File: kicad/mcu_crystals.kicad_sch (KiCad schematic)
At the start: 4 parts, among them X1 32MHz, X2 32kHz768

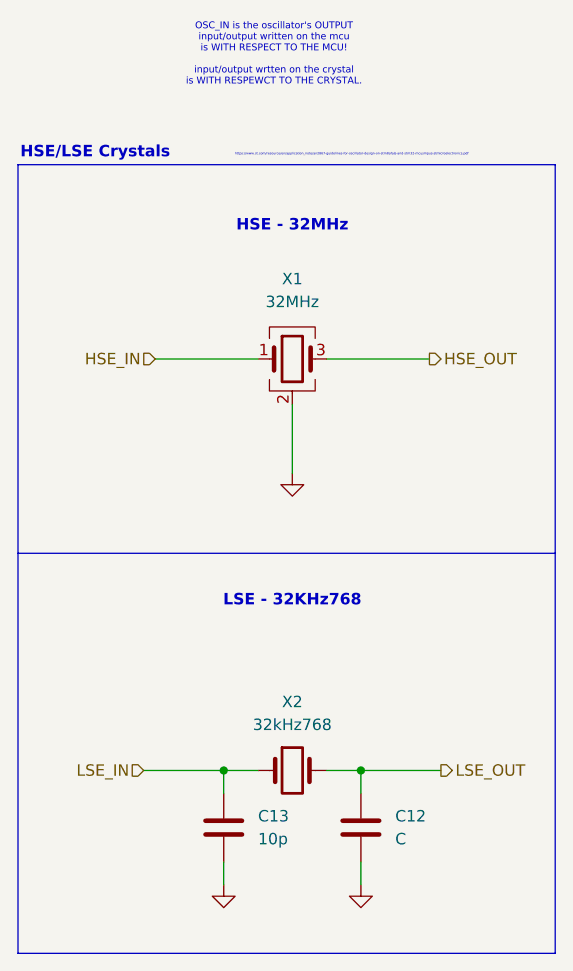
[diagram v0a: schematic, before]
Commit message: refactor(schematic): polish the schematic as much as possible - add new Basmala - fix netlist names almost EVERYWHERE, this is to help with net classes, and to help with building a good habit of naming nets properly - add a 100n capacitor to the SWD connector power pin - update many many other things EVERYWHERE
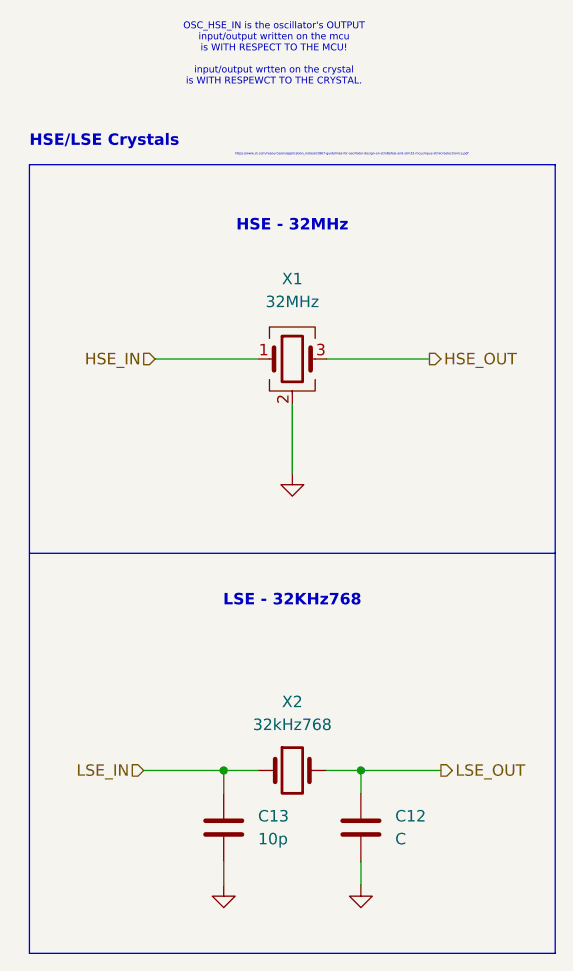
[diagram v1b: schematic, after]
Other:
- note added: "OSC_HSE_IN is the oscillator's OUTPUT input/output written on the mcu is WITH RESPECT TO THE MCU! input/output wrtten on the crystal is WITH RESPEWCT TO THE CRYSTAL."
- note removed: "OSC_IN is the oscillator's OUTPUT input/output written on the mcu is WITH RESPECT TO THE MCU! input/output wrtten on the crystal is WITH RESPEWCT TO THE CRYSTAL."
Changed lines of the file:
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@@
 	)
 	(rectangle
-		(start 125.73 58.42)
+		(start 127 58.42)
 		(end 185.42 146.05)
 		(stroke
@@
 	(text "HSE/LSE Crystals"
 		(exclude_from_sim no)
-		(at 125.984 57.15 0)
+		(at 127 55.88 0)
 		(effects
 			(font
@@
 		)
 	)
-	(text "OSC_IN is the oscillator's OUTPUT\ninput/output written on the mcu\nis WITH RESPECT TO THE MCU!\n\ninput/output wrtten on the crystal\nis WITH RESPEWCT TO THE CRYSTAL."
+	(text "OSC_HSE_IN is the oscillator's OUTPUT\ninput/output written on the mcu\nis WITH RESPECT TO THE MCU!\n\ninput/output wrtten on the crystal\nis WITH RESPEWCT TO THE CRYSTAL."
 		(exclude_from_sim no)
 		(at 154.178 46.228 0)
@@
 	(polyline
 		(pts
-			(xy 125.73 101.6) (xy 185.42 101.6)
+			(xy 127 101.6) (xy 185.42 101.6)
 		)
 		(stroke
